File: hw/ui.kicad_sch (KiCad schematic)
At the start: 0 parts

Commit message: Schematic updates.
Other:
- company: (none) -> AESilky
- title: (none) -> MuKOB - Device
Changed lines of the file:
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@@
 (kicad_sch (version 20230121) (generator eeschema)
-  (paper "A4")
+  (paper "A")
+  (title_block
+    (title "MuKOB - Device")
+    (date "2023-05-25")
+    (rev "1")
+    (company "AESilky")
+    (comment 1 "Copyright 2023 AESilky")
+  )
 )

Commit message: Update and organize display component docs.
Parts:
- added DISP-1: ~, symbol Display_Panel_SPI_I2C:TFT_SPI_TP_SD_35
- added H1, H2, H3, H4: MountingHole, MountingHole:MountingHole_2.7mm_M2.5, symbol Mechanical:MountingHole
- added J12: Conn_01x03, symbol Connector_Generic:Conn_01x03
- added J13: Conn_01x06, symbol Connector_Generic:Conn_01x06
- added RE1: RotaryEncoder_Switch, symbol Device:RotaryEncoder_Switch
- added SW1: SP-2, Button_Switch_SMD:SW_Push_1P1T_NO_Vertical_Wuerth_434133025816, symbol Switch:SW_Push
- added SW1: SP-1, Button_Switch_SMD:SW_Push_1P1T_NO_Vertical_Wuerth_434133025816, symbol Switch:SW_Push
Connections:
- new net: DISP-1.8 (LED_BL), J12.2 (Pin_2)
- new net: DISP-1.SD1 (SD_CS-), J13.6 (Pin_6)
- new net: DISP-1.SD2 (SD_MOSI), J13.5 (Pin_5)
- new net: DISP-1.SD3 (SD_MISO), J13.4 (Pin_4)
- new net: DISP-1.SD4 (SD_CLK), J13.3 (Pin_3)
- new net +3.3V: DISP-1.1 (VCC), J12.3 (Pin_3), J13.2 (Pin_2)
- new net GND: DISP-1.2 (GND), J13.1 (Pin_1), RE1.C, RE1.S2, SW1.2, SW1.2
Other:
- note added: "BACKLIGHT SELECT"
- note added: "CLK"
- note added: "CS-"
- note added: "GND"
- note added: "SDA(MOSI)"
- note added: "SDO(MISO)"
- note added: "SPI_SD"
- note added: "VCC"

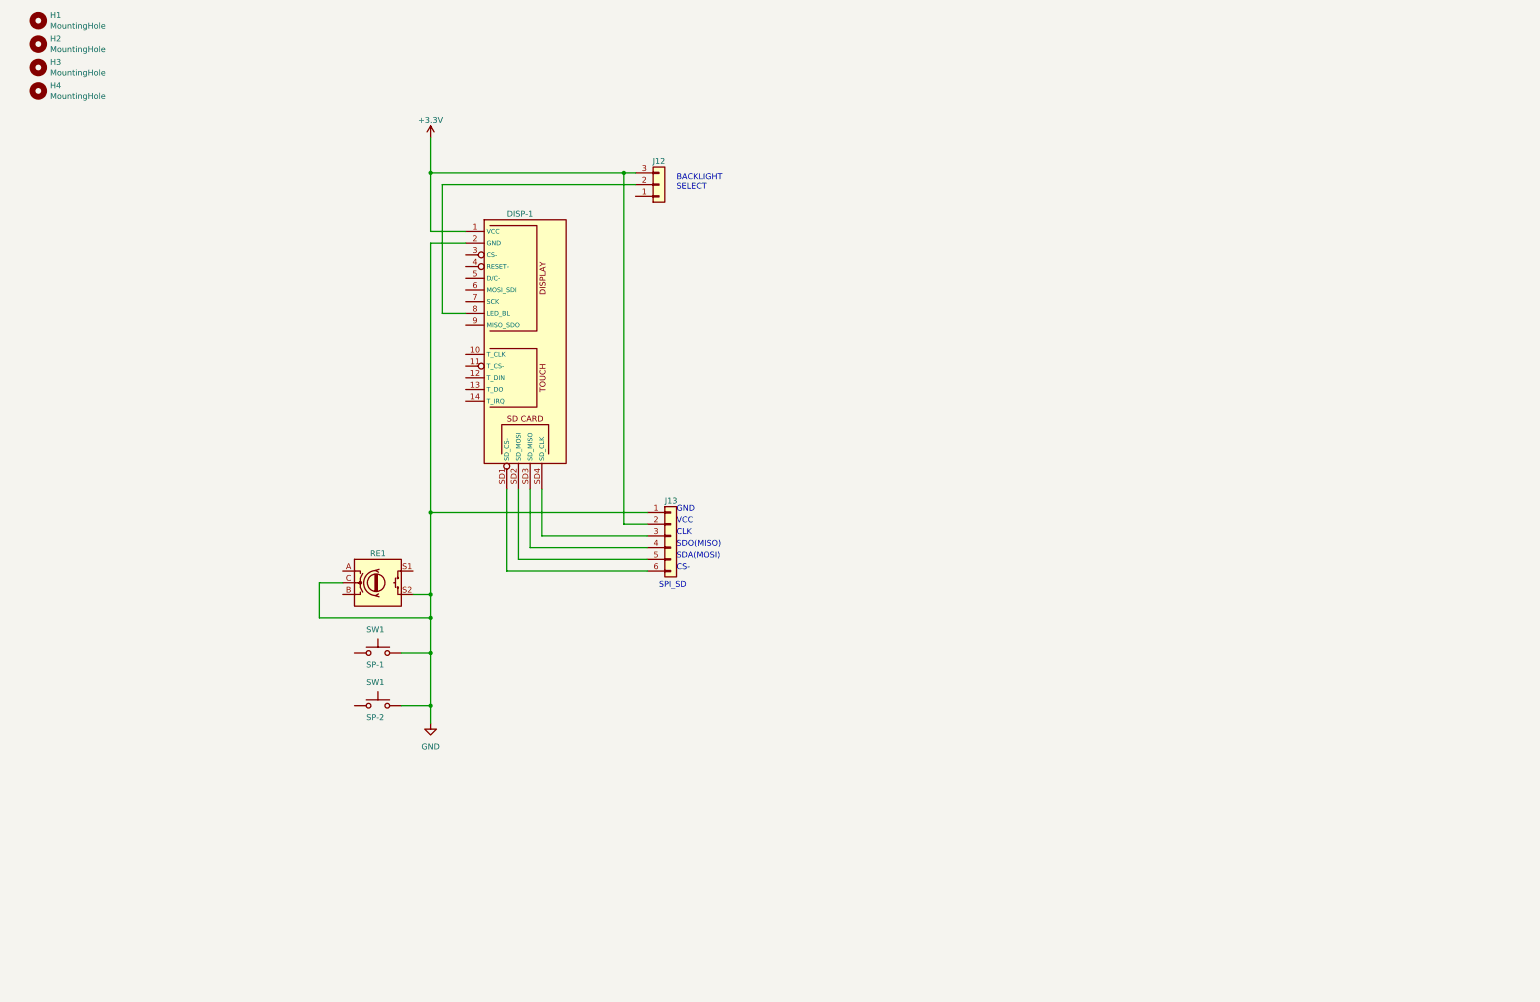
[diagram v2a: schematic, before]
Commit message: HW - Display FFCs.
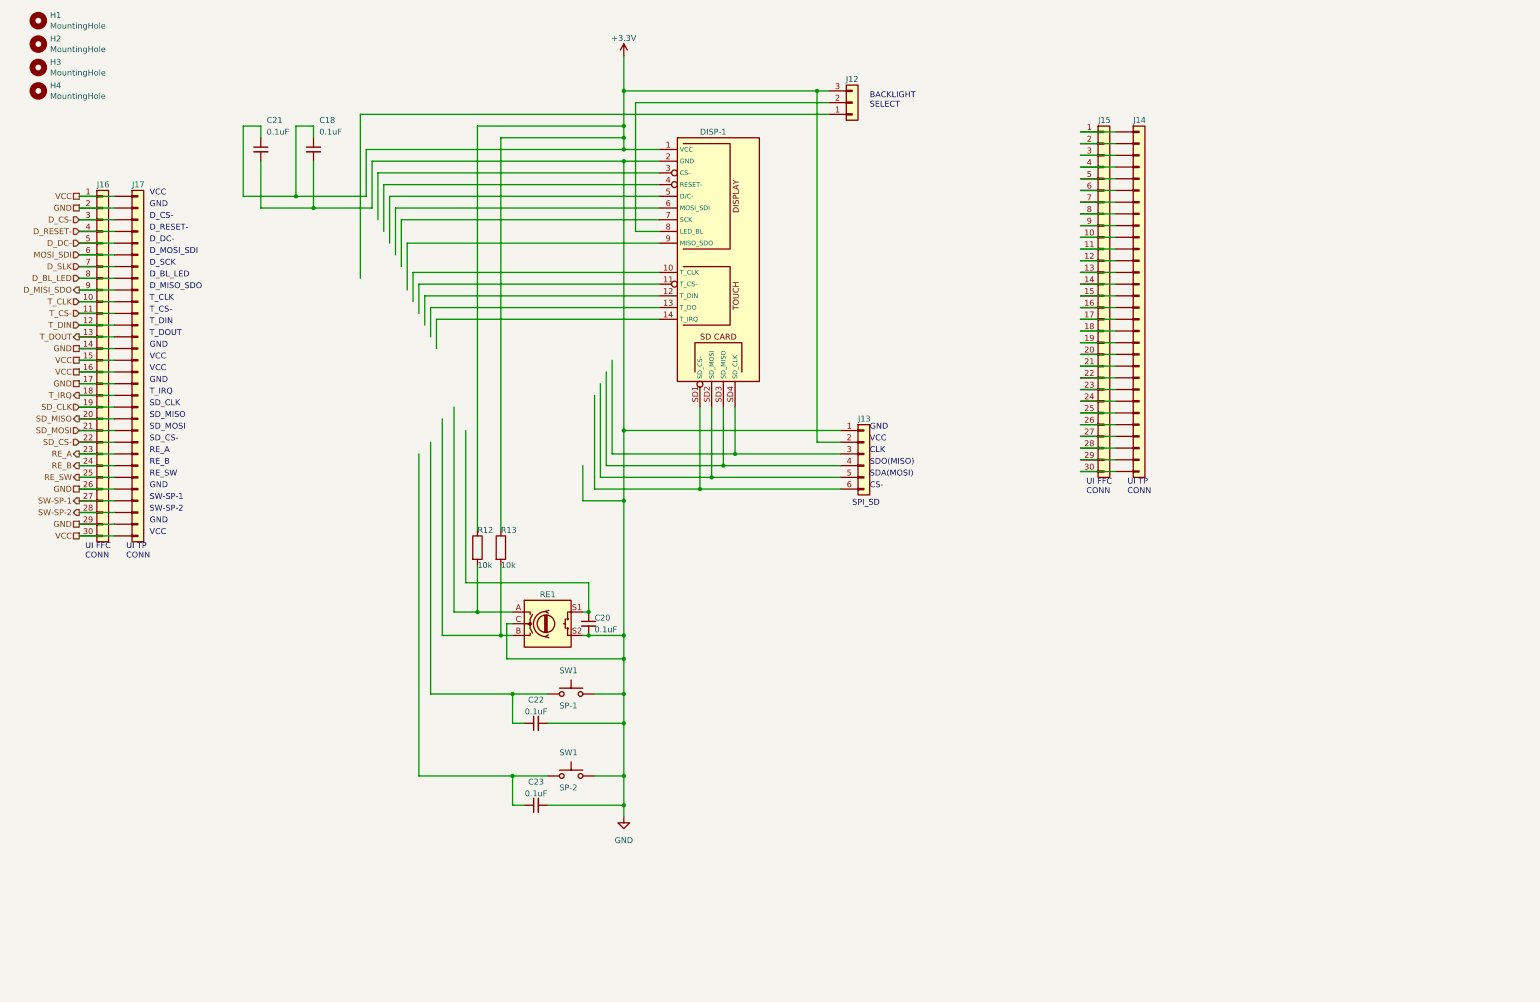
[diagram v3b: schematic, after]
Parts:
- added C18, C20, C21, C22, C23: 0.1uF, symbol Device:C_Small
- added J14, J15, J16, J17: Conn_01x30, symbol Connector_Generic:Conn_01x30
- added R12, R13: 10k, symbol Device:R
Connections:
- net +3.3V: now also C18.1, C21.1, R12.1, R13.1
- net GND: now also C18.2, C20.2, C21.2, C22.2, C23.2, J16.14 (Pin_14), J16.17 (Pin_17), J16.2 (Pin_2), J16.26 (Pin_26), J16.29 (Pin_29), J17.14 (Pin_14), J17.17 (Pin_17), J17.2 (Pin_2), J17.26 (Pin_26), J17.29 (Pin_29)
- net at SW1.1: now also C23.1
- net at RE1.A: now also R12.2
- net at RE1.B: now also R13.2
- net at RE1.S1: now also C20.1
- net at SW1.1: now also C22.1
- new net: J14.1 (Pin_1), J15.1 (Pin_1)
- new net: J14.10 (Pin_10), J15.10 (Pin_10)
- new net: J14.11 (Pin_11), J15.11 (Pin_11)
- new net: J14.12 (Pin_12), J15.12 (Pin_12)
- new net: J14.13 (Pin_13), J15.13 (Pin_13)
- new net: J14.14 (Pin_14), J15.14 (Pin_14)
- new net: J14.15 (Pin_15), J15.15 (Pin_15)
- new net: J14.16 (Pin_16), J15.16 (Pin_16)
- new net: J14.17 (Pin_17), J15.17 (Pin_17)
- new net: J14.18 (Pin_18), J15.18 (Pin_18)
- new net: J14.19 (Pin_19), J15.19 (Pin_19)
- new net: J14.2 (Pin_2), J15.2 (Pin_2)
- new net: J14.20 (Pin_20), J15.20 (Pin_20)
- new net: J14.21 (Pin_21), J15.21 (Pin_21)
- new net: J14.22 (Pin_22), J15.22 (Pin_22)
- new net: J14.23 (Pin_23), J15.23 (Pin_23)
- new net: J14.24 (Pin_24), J15.24 (Pin_24)
- new net: J14.25 (Pin_25), J15.25 (Pin_25)
- new net: J14.26 (Pin_26), J15.26 (Pin_26)
- new net: J14.27 (Pin_27), J15.27 (Pin_27)
- new net: J14.28 (Pin_28), J15.28 (Pin_28)
- new net: J14.29 (Pin_29), J15.29 (Pin_29)
- new net: J14.3 (Pin_3), J15.3 (Pin_3)
- new net: J14.30 (Pin_30), J15.30 (Pin_30)
- new net: J14.4 (Pin_4), J15.4 (Pin_4)
- new net: J14.5 (Pin_5), J15.5 (Pin_5)
- new net: J14.6 (Pin_6), J15.6 (Pin_6)
- new net: J14.7 (Pin_7), J15.7 (Pin_7)
- new net: J14.8 (Pin_8), J15.8 (Pin_8)
- new net: J14.9 (Pin_9), J15.9 (Pin_9)
- new net D_BL_LED: J16.8 (Pin_8), J17.8 (Pin_8)
- new net D_CS-: J16.3 (Pin_3), J17.3 (Pin_3)
- new net D_DC-: J16.5 (Pin_5), J17.5 (Pin_5)
- new net D_MISI_SDO: J16.9 (Pin_9), J17.9 (Pin_9)
- new net D_RESET-: J16.4 (Pin_4), J17.4 (Pin_4)
- new net D_SLK: J16.7 (Pin_7), J17.7 (Pin_7)
- new net MOSI_SDI: J16.6 (Pin_6), J17.6 (Pin_6)
- new net RE_A: J16.23 (Pin_23), J17.23 (Pin_23)
- new net RE_B: J16.24 (Pin_24), J17.24 (Pin_24)
- new net RE_SW: J16.25 (Pin_25), J17.25 (Pin_25)
- new net SD_CLK: J16.19 (Pin_19), J17.19 (Pin_19)
- new net SD_CS-: J16.22 (Pin_22), J17.22 (Pin_22)
- new net SD_MISO: J16.20 (Pin_20), J17.20 (Pin_20)
- new net SD_MOSI: J16.21 (Pin_21), J17.21 (Pin_21)
- new net SW-SP-1: J16.27 (Pin_27), J17.27 (Pin_27)
- new net SW-SP-2: J16.28 (Pin_28), J17.28 (Pin_28)
- new net T_CLK: J16.10 (Pin_10), J17.10 (Pin_10)
- new net T_CS-: J16.11 (Pin_11), J17.11 (Pin_11)
- new net T_DIN: J16.12 (Pin_12), J17.12 (Pin_12)
- new net T_DOUT: J16.13 (Pin_13), J17.13 (Pin_13)
- new net T_IRQ: J16.18 (Pin_18), J17.18 (Pin_18)
- new net VCC: J16.1 (Pin_1), J16.15 (Pin_15), J16.16 (Pin_16), J16.30 (Pin_30), J17.1 (Pin_1), J17.15 (Pin_15), J17.16 (Pin_16), J17.30 (Pin_30)
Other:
- note added: "D_BL_LED"
- note added: "D_CS-"
- note added: "D_DC-"
- note added: "D_MISO_SDO"
- note added: "D_MOSI_SDI"
- note added: "D_RESET-"
- note added: "D_SCK"
- note added: "RE_A"
- note added: "RE_B"
- note added: "RE_SW"
- note added: "SD_CLK"
- note added: "SD_CS-"
- note added: "SD_MISO"
- note added: "SD_MOSI"
- note added: "SW-SP-1"
- note added: "SW-SP-2"
- note added: "T_CLK"
- note added: "T_CS-"
- note added: "T_DIN"
- note added: "T_DOUT"
- note added: "T_IRQ"
- note added: "UI FFC CONN"
- note added: "UI TP CONN"
- moved on the sheet: DISP-1, J12, J13, RE1, SW1

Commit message: Finish KOB page. UI FFC on.
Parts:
- removed J14, J15, J17: Conn_01x30, symbol Connector_Generic:Conn_01x30
- added J17: Conn_02x15_Odd_Even, symbol Connector_Generic:Conn_02x15_Odd_Even
- renumbered C21 to CF1, C18 to CF2
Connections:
- net GND is gone; now on net +3.3V: C20.2, C22.2, C23.2, CF1.2, CF2.2, DISP-1.2 (GND), J13.1 (Pin_1), J16.14 (Pin_14), J16.17 (Pin_17), J16.2 (Pin_2), J16.26 (Pin_26), J16.29 (Pin_29), RE1.C, RE1.S2, SW1.2, SW1.2
- net VCC is gone; now on net +3.3V: J16.1 (Pin_1), J16.15 (Pin_15), J16.16 (Pin_16), J16.30 (Pin_30)
- net +3.3V: now also J17.1 (Pin_1), J17.14 (Pin_14), J17.15 (Pin_15), J17.16 (Pin_16), J17.17 (Pin_17), J17.2 (Pin_2), J17.26 (Pin_26), J17.29 (Pin_29), J17.30 (Pin_30)
- net D_BL_LED: now also J12.1 (Pin_1), J17.8 (Pin_8)
- net D_CS-: now also DISP-1.3 (CS-), J17.3 (Pin_3)
- net D_DC-: now also DISP-1.5 (D/C-), J17.5 (Pin_5)
- net D_MISI_SDO: now also DISP-1.9 (MISO_SDO), J17.9 (Pin_9)
- net D_RESET-: now also DISP-1.4 (RESET-), J17.4 (Pin_4)
- net D_SLK: now also DISP-1.7 (SCK), J17.7 (Pin_7)
- net MOSI_SDI: now also DISP-1.6 (MOSI_SDI), J17.6 (Pin_6)
- net RE_A: now also R12.2, RE1.A, J17.23 (Pin_23)
- net RE_B: now also R13.2, RE1.B, J17.24 (Pin_24)
- net RE_SW: now also C20.1, RE1.S1, J17.25 (Pin_25)
- net SD_CLK: now also J17.19 (Pin_19)
- net SD_CS-: now also DISP-1.SD1 (SD_CS-), J13.6 (Pin_6), J17.22 (Pin_22)
- net SD_MISO: now also J17.20 (Pin_20)
- net SD_MOSI: now also J17.21 (Pin_21)
- net SW-SP-1: now also C22.1, SW1.1, J17.27 (Pin_27)
- net SW-SP-2: now also C23.1, SW1.1, J17.28 (Pin_28)
- net T_CLK: now also DISP-1.10 (T_CLK), J17.10 (Pin_10)
- net T_CS-: now also DISP-1.11 (T_CS-), J17.11 (Pin_11)
- net T_DIN: now also DISP-1.12 (T_DIN), J17.12 (Pin_12)
- net T_DOUT: now also DISP-1.13 (T_DO), J17.13 (Pin_13)
- net T_IRQ: now also DISP-1.14 (T_IRQ), J17.18 (Pin_18)
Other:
- note added: "UI FFC"
- note added: "UI RC"
- note removed: "UI FFC CONN"
- note removed: "UI TP CONN"
- moved on the sheet: C20, C22, C23, CF1, CF2, DISP-1, J12, J13, J16, R12, R13, RE1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
